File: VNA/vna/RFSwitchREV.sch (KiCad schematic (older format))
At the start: 2 parts

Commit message: adjusted main schematic to suit initial presentation
i moved a few blocks around so that the cropped version of the block diagram would fit nicely in my semester 1 presentation
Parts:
- gave numbers to parts that had none: 2
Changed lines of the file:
@@
 AR Path="/5CCA873A/5CCAAE88" Ref="SWs?"  Part="1"
 AR Path="/5CCA9268/5CCAAE88" Ref="SWs?"  Part="1"
-AR Path="/5CCA993F/5CCAAE88" Ref="SWs?"  Part="1"
-F 0 "SWs?" H 5200 4050 50  0000 C CNN
+AR Path="/5CCA993F/5CCAAE88" Ref="SWs3"  Part="1"
+F 0 "SWs3" H 5200 4050 50  0000 C CNN
 F 1 "ADG918BRM" H 5700 4150 50  0000 C CNN
 F 2 "Package_SO:MSOP-8_3x3mm_P0.65mm" H 5450 3250 50  0001 C CNN
@@
 AR Path="/5CCA873A/5CCAAE8E" Ref="C?"  Part="1"
 AR Path="/5CCA9268/5CCAAE8E" Ref="C?"  Part="1"
-AR Path="/5CCA993F/5CCAAE8E" Ref="C?"  Part="1"
-F 0 "C?" H 6792 3596 50  0000 L CNN
+AR Path="/5CCA993F/5CCAAE8E" Ref="C3"  Part="1"
+F 0 "C3" H 6792 3596 50  0000 L CNN
 F 1 "10u" H 6792 3505 50  0000 L CNN
 F 2 "" H 6700 3550 50  0001 C CNN
@@
 AR Path="/5CCA873A/5CCAAE97" Ref="#PWR?"  Part="1"
 AR Path="/5CCA9268/5CCAAE97" Ref="#PWR?"  Part="1"
-AR Path="/5CCA993F/5CCAAE97" Ref="#PWR?"  Part="1"
-F 0 "#PWR?" H 5450 4000 50  0001 C CNN
+AR Path="/5CCA993F/5CCAAE97" Ref="#PWR014"  Part="1"
+F 0 "#PWR014" H 5450 4000 50  0001 C CNN
 F 1 "GNDD" H 5454 4095 50  0000 C CNN
 F 2 "" H 5450 4250 50  0001 C CNN
@@
 AR Path="/5CCA873A/5CCAAE9D" Ref="#PWR?"  Part="1"
 AR Path="/5CCA9268/5CCAAE9D" Ref="#PWR?"  Part="1"
-AR Path="/5CCA993F/5CCAAE9D" Ref="#PWR?"  Part="1"
-F 0 "#PWR?" H 5450 3000 50  0001 C CNN
+AR Path="/5CCA993F/5CCAAE9D" Ref="#PWR013"  Part="1"
+F 0 "#PWR013" H 5450 3000 50  0001 C CNN
 F 1 "VDD" H 5467 3323 50  0000 C CNN
 F 2 "" H 5450 3150 50  0001 C CNN

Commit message: micro-controller pins labelled
micro controller pins have been labelled, the pins on the bottom are yet to be linked to them.

still to wire up ftdi chip,

still to decide upon rf switch control schema.
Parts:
- renumbered C3 to C2, SWs3 to SWs2
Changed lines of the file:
@@
 AR Path="/5CCA873A/5CCAAE88" Ref="SWs?"  Part="1"
 AR Path="/5CCA9268/5CCAAE88" Ref="SWs?"  Part="1"
-AR Path="/5CCA993F/5CCAAE88" Ref="SWs3"  Part="1"
-F 0 "SWs3" H 5200 4050 50  0000 C CNN
+AR Path="/5CCA993F/5CCAAE88" Ref="SWs2"  Part="1"
+F 0 "SWs2" H 5200 4050 50  0000 C CNN
 F 1 "ADG918BRM" H 5700 4150 50  0000 C CNN
 F 2 "Package_SO:MSOP-8_3x3mm_P0.65mm" H 5450 3250 50  0001 C CNN
@@
 AR Path="/5CCA873A/5CCAAE8E" Ref="C?"  Part="1"
 AR Path="/5CCA9268/5CCAAE8E" Ref="C?"  Part="1"
-AR Path="/5CCA993F/5CCAAE8E" Ref="C3"  Part="1"
-F 0 "C3" H 6792 3596 50  0000 L CNN
+AR Path="/5CCA993F/5CCAAE8E" Ref="C2"  Part="1"
+F 0 "C2" H 6792 3596 50  0000 L CNN
 F 1 "10u" H 6792 3505 50  0000 L CNN
 F 2 "" H 6700 3550 50  0001 C CNN

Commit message: finished controller, chose compatible switches
controller and rf switches have been completed.

ToDo: finish filter design for RF Source, add auto gain control
ToDo: finish directional coupler footprints
ToDo: PCB Layout
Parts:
- removed C2: 10u, symbol Device:C_Small
- removed SWs2: ADG918BRM, Package_SO:MSOP-8_3x3mm_P0.65mm, symbol RF_Switch:ADG918BRM
- added C4, C5, C6: 100n, Capacitor_SMD:C_0805_2012Metric_Pad1.15x1.40mm_HandSolder, symbol Device:C_Small
- added U1: 74HCT04, Package_SO:SOIC-14_3.9x8.7mm_P1.27mm, symbol 74xx:74HCT04
- added U3: HMC284, Package_SO:MSOP-8-1EP_3x3mm_P0.65mm_EP2.5x3mm_Mask1.73x2.36mm_ThermalVias, symbol vna-rescue:HMC284
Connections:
- net labels added: GND
- net labels removed: GNDD, VDD
- wire segments 6 -> 21
- no-connect marks 0 -> 1
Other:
- note added: "Hex Inverter"
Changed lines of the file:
@@
 $Descr A4 11693 8268
 encoding utf-8
-Sheet 6 10
+Sheet 5 10
 Title ""
 Date ""
@@
 Comment4 ""
 $EndDescr
+Text HLabel 7500 5000 2    50   Input ~ 0
+RevOut
+Text HLabel 7800 2800 2    50   Input ~ 0
+Rev1In
+Text HLabel 6800 2800 0    50   Input ~ 0
+Rev2In
+Text HLabel 5700 4700 0    50   Input ~ 0
+Ctrl
 $Comp
-L RF_Switch:ADG918BRM SWs?
-U 1 1 5CCAAE88
-P 5450 3700
-AR Path="/5CCAAE88" Ref="SWs?"  Part="1"
-AR Path="/5CC6DDE1/5CCAAE88" Ref="SWs?"  Part="1"
-AR Path="/5CCA83E4/5CCAAE88" Ref="SWs?"  Part="1"
-AR Path="/5CCA873A/5CCAAE88" Ref="SWs?"  Part="1"
-AR Path="/5CCA9268/5CCAAE88" Ref="SWs?"  Part="1"
-AR Path="/5CCA993F/5CCAAE88" Ref="SWs2"  Part="1"
-F 0 "SWs2" H 5200 4050 50  0000 C CNN
-F 1 "ADG918BRM" H 5700 4150 50  0000 C CNN
-F 2 "Package_SO:MSOP-8_3x3mm_P0.65mm" H 5450 3250 50  0001 C CNN
-F 3 "https://www.analog.com/media/en/technical-documentation/data-sheets/ADG918_919.pdf" H 5400 3900 50  0001 C CNN
-	1    5450 3700
+L vna-rescue:HMC284 U?
+U 1 1 5D8644E5
+P 7350 3950
+AR Path="/5CC6DDE1/5D8644E5" Ref="U?"  Part="1"
+AR Path="/5CCA83E4/5D8644E5" Ref="U?"  Part="1"
+AR Path="/5CCA993F/5D8644E5" Ref="U3"  Part="1"
+F 0 "U3" H 7728 4021 50  0000 L CNN
+F 1 "HMC284" H 7728 3930 50  0000 L CNN
+F 2 "Package_SO:MSOP-8-1EP_3x3mm_P0.65mm_EP2.5x3mm_Mask1.73x2.36mm_ThermalVias" H 7100 4000 50  0001 C CNN
+F 3 "" H 7100 4000 50  0001 C CNN
+	1    7350 3950
+	1    0    0    -1
+$EndComp
+$Comp
+L power:GND #PWR?
+U 1 1 5D8644EB
+P 7350 3200
+AR Path="/5CC6DDE1/5D8644EB" Ref="#PWR?"  Part="1"
+AR Path="/5CCA83E4/5D8644EB" Ref="#PWR?"  Part="1"
+AR Path="/5CCA993F/5D8644EB" Ref="#PWR017"  Part="1"
+F 0 "#PWR017" H 7350 2950 50  0001 C CNN
+F 1 "GND" H 7355 3027 50  0000 C CNN
+F 2 "" H 7350 3200 50  0001 C CNN
+F 3 "" H 7350 3200 50  0001 C CNN
+	1    7350 3200
+	1    0    0    -1
+$EndComp
+Wire Wire Line
+	7250 3400 7250 3200
+Wire Wire Line
+	7250 3200 7350 3200
+Wire Wire Line
+	7350 3200 7450 3200
+Wire Wire Line
+	7450 3200 7450 3400
+Connection ~ 7350 3200
+NoConn ~ 7600 4450
+$Comp
+L Device:C_Small C?
+U 1 1 5D8644F7
+P 7450 4650
+AR Path="/5CC6DDE1/5D8644F7" Ref="C?"  Part="1"
+AR Path="/5CCA83E4/5D8644F7" Ref="C?"  Part="1"
+AR Path="/5CCA993F/5D8644F7" Ref="C6"  Part="1"
+F 0 "C6" H 7542 4696 50  0000 L CNN
+F 1 "100n" H 7542 4605 50  0000 L CNN
+F 2 "Capacitor_SMD:C_0805_2012Metric_Pad1.15x1.40mm_HandSolder" H 7450 4650 50  0001 C CNN
+F 3 "~" H 7450 4650 50  0001 C CNN
+	1    7450 4650
+	1    0    0    -1
+$EndComp
+Wire Wire Line
+	7450 4450 7450 4550
+$Comp
+L Device:C_Small C?
+U 1 1 5D8644FE
+P 6800 3100
+AR Path="/5CC6DDE1/5D8644FE" Ref="C?"  Part="1"
+AR Path="/5CCA83E4/5D8644FE" Ref="C?"  Part="1"
+AR Path="/5CCA993F/5D8644FE" Ref="C4"  Part="1"
+F 0 "C4" H 6892 3146 50  0000 L CNN
+F 1 "100n" H 6892 3055 50  0000 L CNN
+F 2 "Capacitor_SMD:C_0805_2012Metric_Pad1.15x1.40mm_HandSolder" H 6800 3100 50  0001 C CNN
+F 3 "~" H 6800 3100 50  0001 C CNN
+	1    6800 3100
 	1    0    0    -1
 $EndComp
 $Comp
 L Device:C_Small C?
-U 1 1 5CCAAE8E
-P 6700 3550
-AR Path="/5CCAAE8E" Ref="C?"  Part="1"
-AR Path="/5CC6DDE1/5CCAAE8E" Ref="C?"  Part="1"
-AR Path="/5CCA83E4/5CCAAE8E" Ref="C?"  Part="1"
-AR Path="/5CCA873A/5CCAAE8E" Ref="C?"  Part="1"
-AR Path="/5CCA9268/5CCAAE8E" Ref="C?"  Part="1"
-AR Path="/5CCA993F/5CCAAE8E" Ref="C2"  Part="1"
-F 0 "C2" H 6792 3596 50  0000 L CNN
-F 1 "10u" H 6792 3505 50  0000 L CNN
-F 2 "" H 6700 3550 50  0001 C CNN
-F 3 "~" H 6700 3550 50  0001 C CNN
-	1    6700 3550
+U 1 1 5D864504
+P 7800 3100
+AR Path="/5CC6DDE1/5D864504" Ref="C?"  Part="1"
+AR Path="/5CCA83E4/5D864504" Ref="C?"  Part="1"
+AR Path="/5CCA993F/5D864504" Ref="C5"  Part="1"
+F 0 "C5" H 7892 3146 50  0000 L CNN
+F 1 "100n" H 7892 3055 50  0000 L CNN
+F 2 "Capacitor_SMD:C_0805_2012Metric_Pad1.15x1.40mm_HandSolder" H 7800 3100 50  0001 C CNN
+F 3 "~" H 7800 3100 50  0001 C CNN
+	1    7800 3100
 	1    0    0    -1
 $EndComp
-Text HLabel 4950 3600 0    50   Input ~ 0
-RevOut
-Text HLabel 5950 3500 2    50   Input ~ 0
-Rev1In
-Text HLabel 5950 3700 2    50   Input ~ 0
-Rev2In
+Wire Wire Line
+	7600 3400 7800 3400
+Wire Wire Line
+	7800 3400 7800 3200
+Wire Wire Line
+	7100 3400 6800 3400
+Wire Wire Line
+	6800 3400 6800 3200
+Wire Wire Line
+	6800 3000 6800 2800
 $Comp
-L power:GNDD #PWR?
-U 1 1 5CCAAE97
-P 5450 4250
-AR Path="/5CC6DDE1/5CCAAE97" Ref="#PWR?"  Part="1"
-AR Path="/5CCA83E4/5CCAAE97" Ref="#PWR?"  Part="1"
-AR Path="/5CCA873A/5CCAAE97" Ref="#PWR?"  Part="1"
-AR Path="/5CCA9268/5CCAAE97" Ref="#PWR?"  Part="1"
-AR Path="/5CCA993F/5CCAAE97" Ref="#PWR014"  Part="1"
-F 0 "#PWR014" H 5450 4000 50  0001 C CNN
-F 1 "GNDD" H 5454 4095 50  0000 C CNN
-F 2 "" H 5450 4250 50  0001 C CNN
-F 3 "" H 5450 4250 50  0001 C CNN
-	1    5450 4250
+L 74xx:74HCT04 U?
+U 5 1 5D86450F
+P 6200 4700
+AR Path="/5CC6DDE1/5D86450F" Ref="U?"  Part="1"
+AR Path="/5CCA83E4/5D86450F" Ref="U?"  Part="3"
+AR Path="/5CCA993F/5D86450F" Ref="U1"  Part="5"
+F 0 "U1" H 6200 4500 50  0000 C CNN
+F 1 "74HCT04" H 6200 4400 50  0000 C CNN
+F 2 "Package_SO:SOIC-14_3.9x8.7mm_P1.27mm" H 6200 4700 50  0001 C CNN
+F 3 "https://assets.nexperia.com/documents/data-sheet/74HC_HCT04.pdf" H 6200 4700 50  0001 C CNN
+	5    6200 4700
 	1    0    0    -1
 $EndComp
 $Comp
-L power:VDD #PWR?
-U 1 1 5CCAAE9D
-P 5450 3150
-AR Path="/5CC6DDE1/5CCAAE9D" Ref="#PWR?"  Part="1"
-AR Path="/5CCA83E4/5CCAAE9D" Ref="#PWR?"  Part="1"
-AR Path="/5CCA873A/5CCAAE9D" Ref="#PWR?"  Part="1"
-AR Path="/5CCA9268/5CCAAE9D" Ref="#PWR?"  Part="1"
-AR Path="/5CCA993F/5CCAAE9D" Ref="#PWR013"  Part="1"
-F 0 "#PWR013" H 5450 3000 50  0001 C CNN
-F 1 "VDD" H 5467 3323 50  0000 C CNN
-F 2 "" H 5450 3150 50  0001 C CNN
-F 3 "" H 5450 3150 50  0001 C CNN
-	1    5450 3150
+L 74xx:74HCT04 U?
+U 6 1 5D864515
+P 6850 5350
+AR Path="/5CC6DDE1/5D864515" Ref="U?"  Part="2"
+AR Path="/5CCA83E4/5D864515" Ref="U?"  Part="4"
+AR Path="/5CCA993F/5D864515" Ref="U1"  Part="6"
+F 0 "U1" H 6850 5667 50  0000 C CNN
+F 1 "74HCT04" H 6850 5576 50  0000 C CNN
+F 2 "Package_SO:SOIC-14_3.9x8.7mm_P1.27mm" H 6850 5350 50  0001 C CNN
+F 3 "https://assets.nexperia.com/documents/data-sheet/74HC_HCT04.pdf" H 6850 5350 50  0001 C CNN
+	6    6850 5350
 	1    0    0    -1
 $EndComp
-Text HLabel 4950 3800 0    50   Input ~ 0
-Ctrl
 Wire Wire Line
-	5450 3150 6700 3150
+	6500 4700 6500 4950
 Wire Wire Line
-	6700 3150 6700 3450
+	6500 5350 6550 5350
 Wire Wire Line
-	5450 3150 5450 3200
-Connection ~ 5450 3150
+	6500 4950 7100 4950
 Wire Wire Line
-	5450 4200 5450 4250
+	7100 4950 7100 4450
+Connection ~ 6500 4950
 Wire Wire Line
-	5450 4250 6700 4250
+	6500 4950 6500 5350
 Wire Wire Line
-	6700 3650 6700 4250
-Connection ~ 5450 4250
-Text GLabel 6100 3150 1    50   Input ~ 0
-VDD
-Text GLabel 6100 4250 3    50   Input ~ 0
-GNDD
+	7150 5350 7250 5350
+Wire Wire Line
+	7250 5350 7250 4450
+Wire Wire Line
+	5700 4700 5900 4700
+Wire Wire Line
+	7800 3000 7800 2800
+Wire Wire Line
+	7450 5000 7500 5000
+Wire Wire Line
+	7450 4750 7450 5000
+Text Notes 5950 5200 0    50   ~ 0
+Hex Inverter
+Wire Notes Line
+	5800 4500 5800 5600
+Wire Notes Line
+	5800 5600 7350 5600
+Wire Notes Line
+	7350 5600 7350 4500
+Wire Notes Line
+	7350 4500 5800 4500
 $EndSCHEMATC

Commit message: custom footprint for couplers, added decoupling caps
added custom footprint for directional couplers - will need to verify it

added decoupling caps to ad9851
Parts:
- C4, C5, C6: footprint Capacitor_SMD:C_0805_2012Metric_Pad1.15x1.40mm_HandSolder -> Capacitor_SMD:C_1206_3216Metric_Pad1.42x1.75mm_HandSolder
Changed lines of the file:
@@
 F 0 "C6" H 7542 4696 50  0000 L CNN
 F 1 "100n" H 7542 4605 50  0000 L CNN
-F 2 "Capacitor_SMD:C_0805_2012Metric_Pad1.15x1.40mm_HandSolder" H 7450 4650 50  0001 C CNN
+F 2 "Capacitor_SMD:C_1206_3216Metric_Pad1.42x1.75mm_HandSolder" H 7450 4650 50  0001 C CNN
 F 3 "~" H 7450 4650 50  0001 C CNN
 	1    7450 4650
@@
 F 0 "C4" H 6892 3146 50  0000 L CNN
 F 1 "100n" H 6892 3055 50  0000 L CNN
-F 2 "Capacitor_SMD:C_0805_2012Metric_Pad1.15x1.40mm_HandSolder" H 6800 3100 50  0001 C CNN
+F 2 "Capacitor_SMD:C_1206_3216Metric_Pad1.42x1.75mm_HandSolder" H 6800 3100 50  0001 C CNN
 F 3 "~" H 6800 3100 50  0001 C CNN
 	1    6800 3100
@@
 F 0 "C5" H 7892 3146 50  0000 L CNN
 F 1 "100n" H 7892 3055 50  0000 L CNN
-F 2 "Capacitor_SMD:C_0805_2012Metric_Pad1.15x1.40mm_HandSolder" H 7800 3100 50  0001 C CNN
+F 2 "Capacitor_SMD:C_1206_3216Metric_Pad1.42x1.75mm_HandSolder" H 7800 3100 50  0001 C CNN
 F 3 "~" H 7800 3100 50  0001 C CNN
 	1    7800 3100

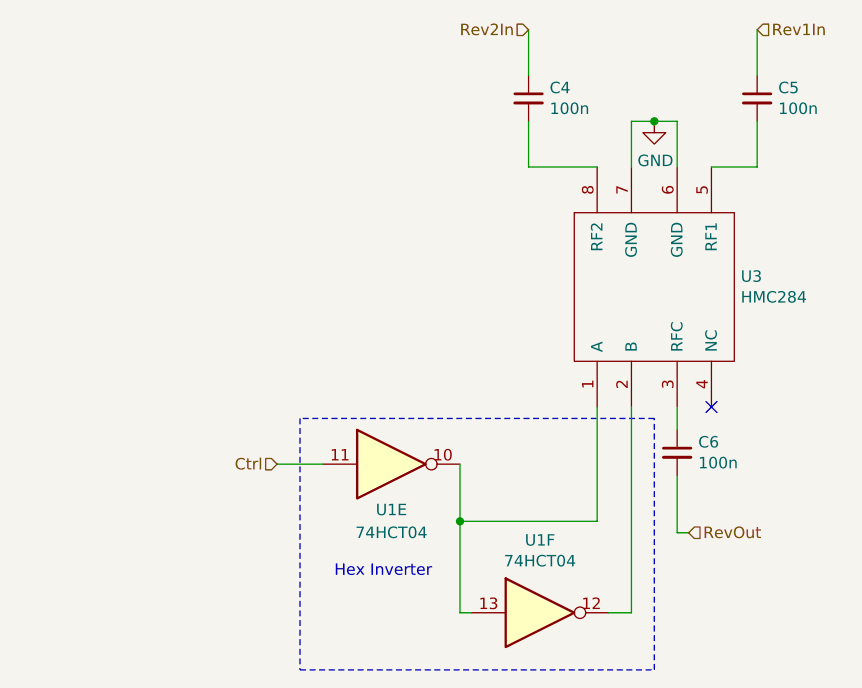
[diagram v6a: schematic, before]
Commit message: initial pcb design
initial layout and grouping of components complete
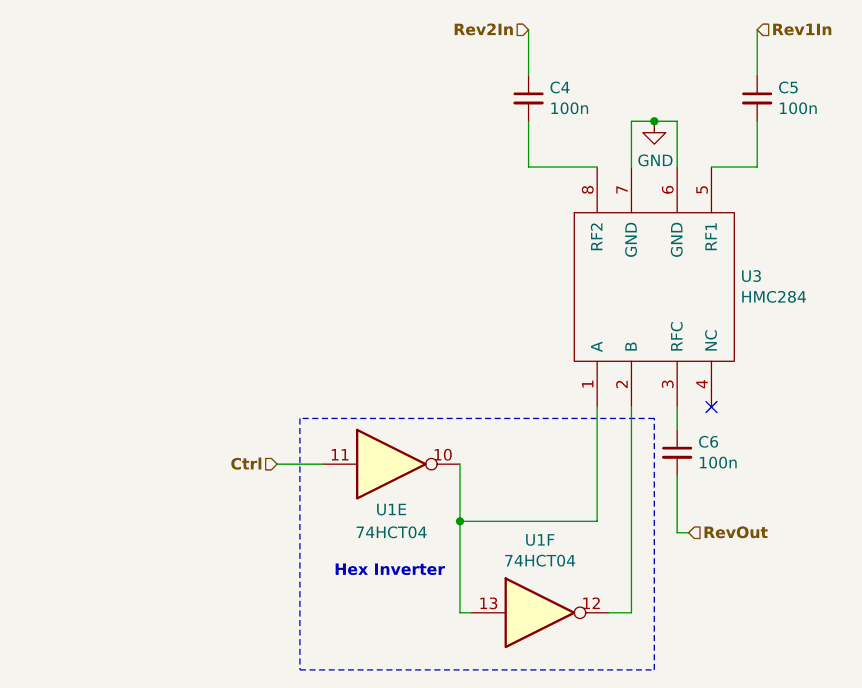
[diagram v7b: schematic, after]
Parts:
- C4, C5, C6: footprint Capacitor_SMD:C_1206_3216Metric_Pad1.42x1.75mm_HandSolder -> Capacitor_SMD:C_0805_2012Metric_Pad1.15x1.40mm_HandSolder
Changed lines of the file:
@@
 $Descr A4 11693 8268
 encoding utf-8
-Sheet 5 10
-Title ""
-Date ""
-Rev ""
-Comp ""
+Sheet 4 10
+Title "Rev Switch"
+Date "2019-09-25"
+Rev "0.1"
+Comp "Benjamin Jackson"
 Comment1 ""
 Comment2 ""
@@
 Comment4 ""
 $EndDescr
-Text HLabel 7500 5000 2    50   Input ~ 0
+Text HLabel 7500 5000 2    50   Input ~ 10
 RevOut
-Text HLabel 7800 2800 2    50   Input ~ 0
+Text HLabel 7800 2800 2    50   Input ~ 10
 Rev1In
-Text HLabel 6800 2800 0    50   Input ~ 0
+Text HLabel 6800 2800 0    50   Input ~ 10
 Rev2In
-Text HLabel 5700 4700 0    50   Input ~ 0
+Text HLabel 5700 4700 0    50   Input ~ 10
 Ctrl
 $Comp
@@
 F 0 "C6" H 7542 4696 50  0000 L CNN
 F 1 "100n" H 7542 4605 50  0000 L CNN
-F 2 "Capacitor_SMD:C_1206_3216Metric_Pad1.42x1.75mm_HandSolder" H 7450 4650 50  0001 C CNN
+F 2 "Capacitor_SMD:C_0805_2012Metric_Pad1.15x1.40mm_HandSolder" H 7450 4650 50  0001 C CNN
 F 3 "~" H 7450 4650 50  0001 C CNN
 	1    7450 4650
@@
 F 0 "C4" H 6892 3146 50  0000 L CNN
 F 1 "100n" H 6892 3055 50  0000 L CNN
-F 2 "Capacitor_SMD:C_1206_3216Metric_Pad1.42x1.75mm_HandSolder" H 6800 3100 50  0001 C CNN
+F 2 "Capacitor_SMD:C_0805_2012Metric_Pad1.15x1.40mm_HandSolder" H 6800 3100 50  0001 C CNN
 F 3 "~" H 6800 3100 50  0001 C CNN
 	1    6800 3100
@@
 F 0 "C5" H 7892 3146 50  0000 L CNN
 F 1 "100n" H 7892 3055 50  0000 L CNN
-F 2 "Capacitor_SMD:C_1206_3216Metric_Pad1.42x1.75mm_HandSolder" H 7800 3100 50  0001 C CNN
+F 2 "Capacitor_SMD:C_0805_2012Metric_Pad1.15x1.40mm_HandSolder" H 7800 3100 50  0001 C CNN
 F 3 "~" H 7800 3100 50  0001 C CNN
 	1    7800 3100
@@
 Wire Wire Line
 	7450 4750 7450 5000
-Text Notes 5950 5200 0    50   ~ 0
+Text Notes 5950 5200 0    50   ~ 10
 Hex Inverter
 Wire Notes Line

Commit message: v0.1 completed, producing gerbers
gerbers to be sent to jlc pcb pending their acceptance, they will be produced
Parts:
- U1: footprint Package_SO:SOIC-14_3.9x8.7mm_P1.27mm -> Package_DIP:DIP-14_W10.16mm
- U3: footprint Package_SO:MSOP-8-1EP_3x3mm_P0.65mm_EP2.5x3mm_Mask1.73x2.36mm_ThermalVias -> Package_SO:MSOP-8-1EP_3x3mm_P0.65mm_EP2.5x3mm_Mask1.73x2.36mm
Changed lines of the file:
@@
 F 0 "U3" H 7728 4021 50  0000 L CNN
 F 1 "HMC284" H 7728 3930 50  0000 L CNN
-F 2 "Package_SO:MSOP-8-1EP_3x3mm_P0.65mm_EP2.5x3mm_Mask1.73x2.36mm_ThermalVias" H 7100 4000 50  0001 C CNN
+F 2 "Package_SO:MSOP-8-1EP_3x3mm_P0.65mm_EP2.5x3mm_Mask1.73x2.36mm" H 7100 4000 50  0001 C CNN
 F 3 "" H 7100 4000 50  0001 C CNN
 	1    7350 3950
@@
 F 0 "U1" H 6200 4500 50  0000 C CNN
 F 1 "74HCT04" H 6200 4400 50  0000 C CNN
-F 2 "Package_SO:SOIC-14_3.9x8.7mm_P1.27mm" H 6200 4700 50  0001 C CNN
+F 2 "Package_DIP:DIP-14_W10.16mm" H 6200 4700 50  0001 C CNN
 F 3 "https://assets.nexperia.com/documents/data-sheet/74HC_HCT04.pdf" H 6200 4700 50  0001 C CNN
 	5    6200 4700
@@
 F 0 "U1" H 6850 5667 50  0000 C CNN
 F 1 "74HCT04" H 6850 5576 50  0000 C CNN
-F 2 "Package_SO:SOIC-14_3.9x8.7mm_P1.27mm" H 6850 5350 50  0001 C CNN
+F 2 "Package_DIP:DIP-14_W10.16mm" H 6850 5350 50  0001 C CNN
 F 3 "https://assets.nexperia.com/documents/data-sheet/74HC_HCT04.pdf" H 6850 5350 50  0001 C CNN
 	6    6850 5350
